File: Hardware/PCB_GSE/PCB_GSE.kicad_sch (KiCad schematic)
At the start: 0 parts

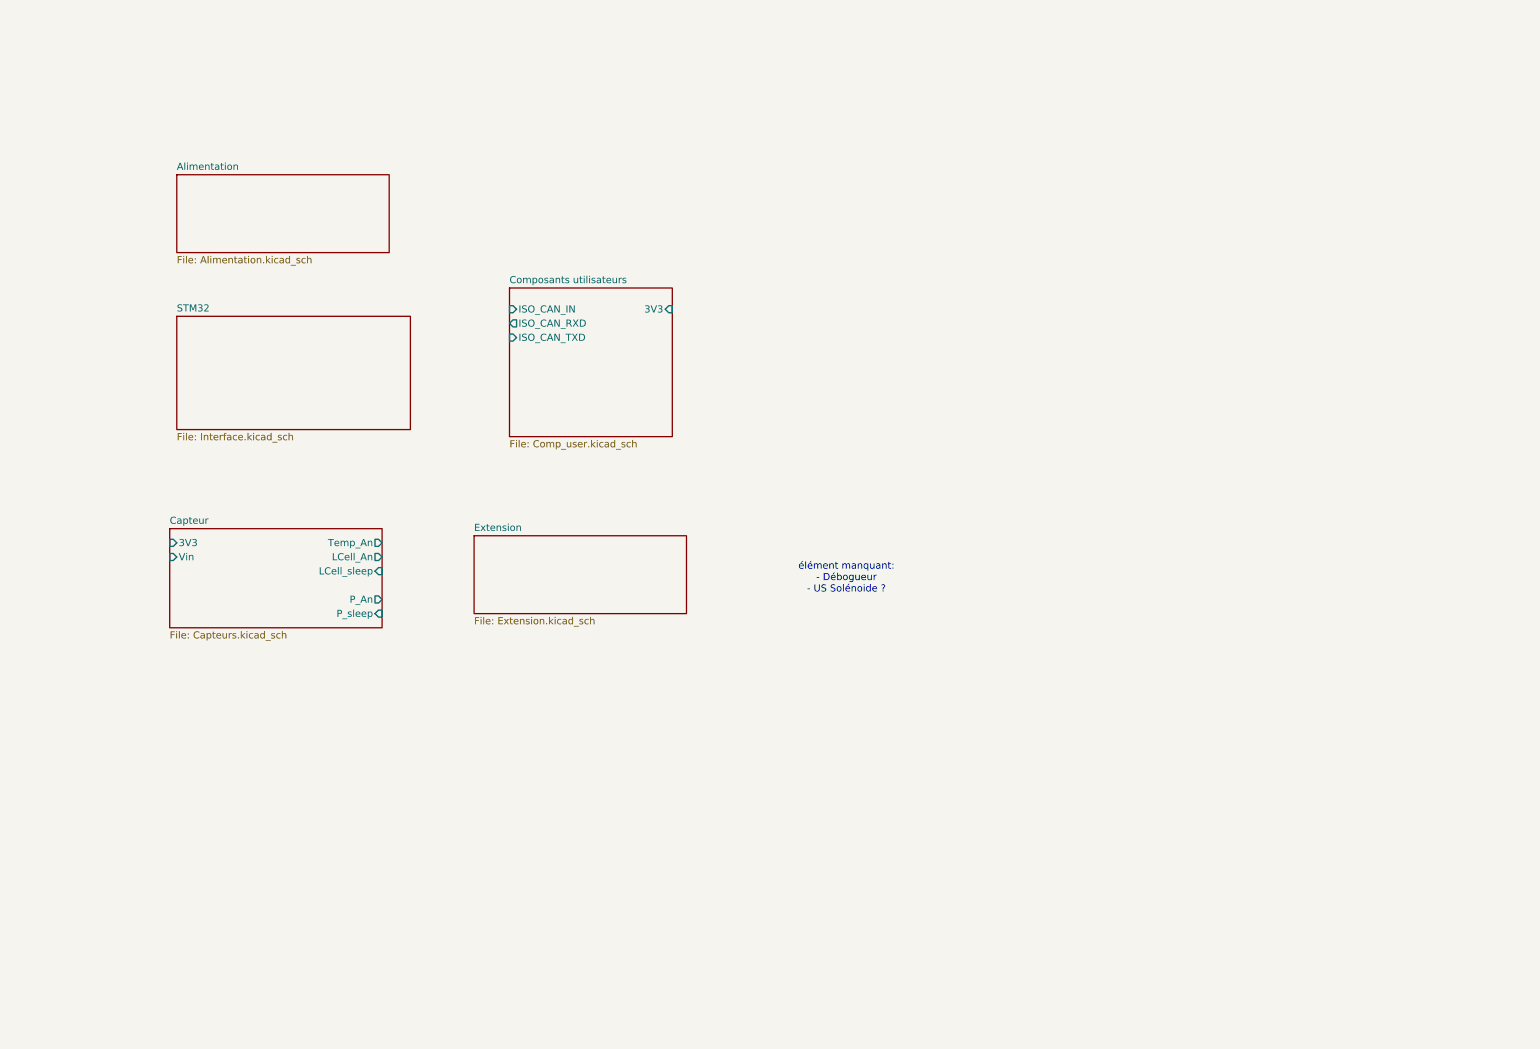
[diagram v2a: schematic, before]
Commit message: feat: copy all existing schematics in gse project + add missing components + fix voltage divider for 3S + create gse project and seperate stm32 project + add missing resistors motor
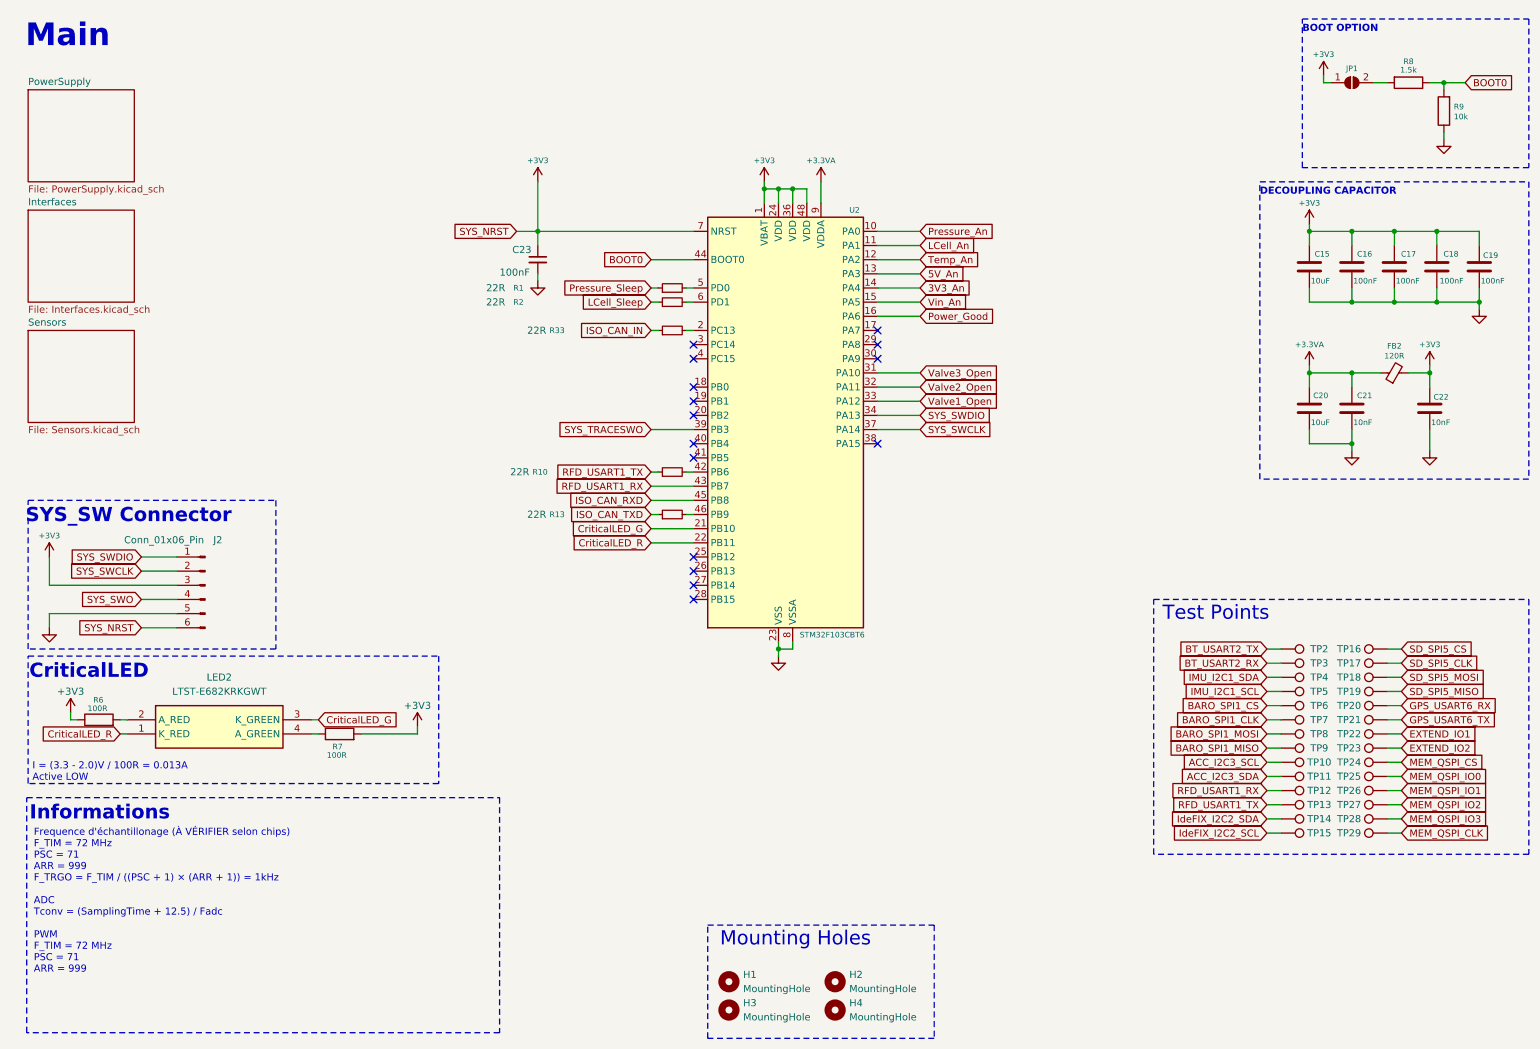
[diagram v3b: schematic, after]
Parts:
- added C15, C20: 10uF, Capacitor_SMD:C_0805_2012Metric, symbol Device:C
- added C16, C17, C18, C19: 100nF, Capacitor_SMD:C_0805_2012Metric, symbol Device:C
- added C21, C22: 10nF, Capacitor_SMD:C_0603_1608Metric, symbol Device:C
- added C23: 100nF, Capacitor_SMD:C_0805_2012Metric, symbol Device:C_Small
- added FB2: 120R, Inductor_SMD:L_0805_2012Metric, symbol Device:FerriteBead_Small
- added H1, H2, H3, H4: MountingHole, MountingHole:MountingHole_4.3mm_M4, symbol Mechanical:MountingHole
- added J2: Conn_01x06_Pin, Connector_PinHeader_2.54mm:PinHeader_1x06_P2.54mm_Vertical, symbol Connector:Conn_01x06_Pin
- added JP1: SolderJumper_2_Open, Jumper:SolderJumper-2_P1.3mm_Open_TrianglePad1.0x1.5mm, symbol Jumper:SolderJumper_2_Open
- added LED2: LTST-E682KRKGWT, LTSTE683RGBW, symbol PCB_GSE:LTST-E682KRKGWT
- added R1, R10, R13, R2, R33: 22R, Resistor_SMD:R_0603_1608Metric, symbol Device:R_Small
- added R6, R7: 100R, Resistor_SMD:R_0805_2012Metric, symbol Device:R
- added R8: 1.5k, Resistor_SMD:R_0603_1608Metric, symbol Device:R
- added R9: 10k, Resistor_SMD:R_0603_1608Metric, symbol Device:R
- added TP10, TP11, TP12, TP13, TP14, TP15, TP16, TP17, TP18, TP19, TP2, TP20, TP21, TP22, TP23, TP24, TP25, TP26, TP27, TP28, TP29, TP3, TP4, TP5, TP6, TP7, TP8, TP9: TestPoint, TestPoint:TestPoint_Pad_D1.0mm, symbol Connector:TestPoint
- added U2: STM32F103CBT6, Package_QFP:LQFP-48_7x7mm_P0.5mm, symbol MCU_ST_STM32F1:STM32F103C8Tx
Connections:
- new net: LED2.4 (A_GREEN), R7.1
- new net: R1.2, U2.5 (PD0)
- new net: R33.2, U2.2 (PC13)
- new net: R10.2, U2.42 (PB6)
- new net: R13.2, U2.46 (PB9)
- new net: R2.2, U2.6 (PD1)
- new net: JP1.2 (B), R8.2
- new net: LED2.2 (A_RED), R6.2
- new net +3.3VA: C20.2, C21.2, FB2.1, U2.9 (VDDA)
- new net +3V3: C15.2, C16.2, C17.2, C18.2, C19.2, C22.2, C23.1, FB2.2, J2.3 (Pin_3), J2.6 (Pin_6), JP1.1 (A), R6.1, R7.2, U2.1 (VBAT), U2.24 (VDD), U2.36 (VDD), U2.48 (VDD), U2.7 (NRST)
- new net 3V3_An: U2.14 (PA4)
- new net 5V_An: U2.13 (PA3)
- new net ACC_I2C3_SCL: TP10.1
- new net ACC_I2C3_SDA: TP11.1
- new net BARO_SPI1_CLK: TP7.1
- new net BARO_SPI1_CS: TP6.1
- new net BARO_SPI1_MISO: TP9.1
- new net BARO_SPI1_MOSI: TP8.1
- new net BOOT0: R8.1, R9.2, U2.44 (BOOT0)
- new net BT_USART2_RX: TP3.1
- new net BT_USART2_TX: TP2.1
- new net CriticalLED_G: LED2.3 (K_GREEN), U2.21 (PB10)
- new net CriticalLED_R: LED2.1 (K_RED), U2.22 (PB11)
- new net EXTEND_IO1: TP22.1
- new net EXTEND_IO2: TP23.1
- new net GND: C15.1, C16.1, C17.1, C18.1, C19.1, C20.1, C21.1, C22.1, C23.2, J2.5 (Pin_5), R9.1, U2.23 (VSS), U2.35 (VSS), U2.47 (VSS), U2.8 (VSSA)
- new net GPS_USART6_RX: TP20.1
- new net GPS_USART6_TX: TP21.1
- new net IMU_I2C1_SCL: TP5.1
- new net IMU_I2C1_SDA: TP4.1
- new net ISO_CAN_IN: R33.1
- new net ISO_CAN_RXD: U2.45 (PB8)
- new net ISO_CAN_TXD: R13.1
- new net IdeFIX_I2C2_SCL: TP15.1
- new net IdeFIX_I2C2_SDA: TP14.1
- new net LCell_An: U2.11 (PA1)
- new net LCell_Sleep: R2.1
- new net MEM_QSPI_CLK: TP29.1
- new net MEM_QSPI_CS: TP24.1
- new net MEM_QSPI_IO0: TP25.1
- new net MEM_QSPI_IO1: TP26.1
- new net MEM_QSPI_IO2: TP27.1
- new net MEM_QSPI_IO3: TP28.1
- new net Power_Good: U2.16 (PA6)
- new net Pressure_An: U2.10 (PA0)
- new net Pressure_Sleep: R1.1
- new net RFD_USART1_RX: TP12.1, U2.43 (PB7)
- new net RFD_USART1_TX: R10.1, TP13.1
- new net SD_SPI5_CLK: TP17.1
- new net SD_SPI5_CS: TP16.1
- new net SD_SPI5_MISO: TP19.1
- new net SD_SPI5_MOSI: TP18.1
- new net SYS_SWCLK: J2.2 (Pin_2), U2.37 (PA14)
- new net SYS_SWDIO: J2.1 (Pin_1), U2.34 (PA13)
- new net SYS_SWO: J2.4 (Pin_4)
- new net SYS_TRACESWO: U2.39 (PB3)
- new net Temp_An: U2.12 (PA2)
- new net Valve1_Open: U2.33 (PA12)
- new net Valve2_Open: U2.32 (PA11)
- new net Valve3_Open: U2.31 (PA10)
- new net Vin_An: U2.15 (PA5)
- no-connect marks 0 -> 15
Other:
- removed sheet Alimentation
- removed sheet Capteur
- removed sheet Composants utilisateurs
- removed sheet Extension
- removed sheet STM32
- added sheet Interfaces (Interfaces.kicad_sch)
- added sheet PowerSupply (PowerSupply.kicad_sch)
- added sheet Sensors (Sensors.kicad_sch)
- note added: "BOOT OPTION"
- note added: "CriticalLED"
- note added: "DECOUPLING CAPACITOR"
- note added: "Frequence d'échantillonage (À VÉRIFIER selon chips) F_TIM = 72 MHz PSC = 71 ARR = 999 F_TRGO = F_TIM / ((PSC + 1) × (ARR + 1)) = 1kHz ADC Tconv = (SamplingTime + 12.5) / Fadc PWM F_TIM = 72 MHz PSC = 71 ARR = 999"
- note added: "I = (3.3 - 2.0)V / 100R = 0.013A Active LOW"
- note added: "Informations"
- note added: "Main"
- note added: "Mounting Holes"
- note added: "SYS_SW Connector"
- note added: "Test Points"
- note removed: "élément manquant: - Débogueur - US Solénoide ?"

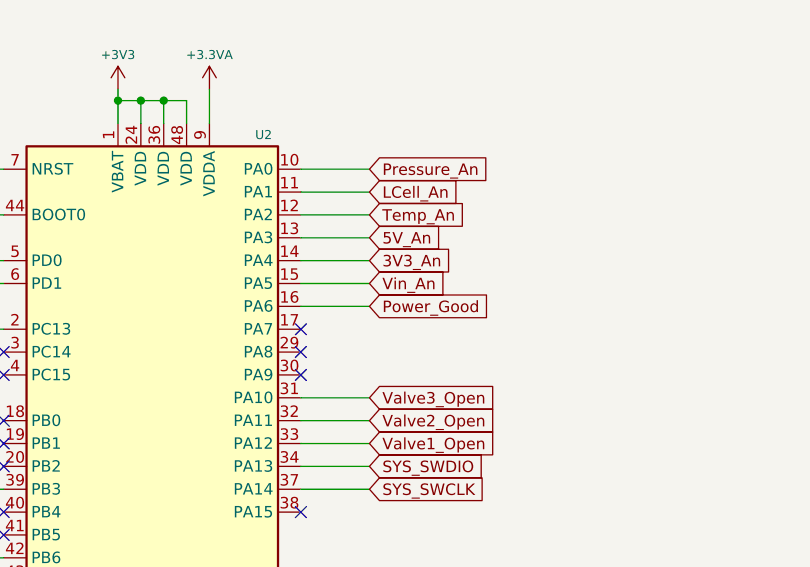
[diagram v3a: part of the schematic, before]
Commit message: fix: stm32 project + modified 12v buck symbol
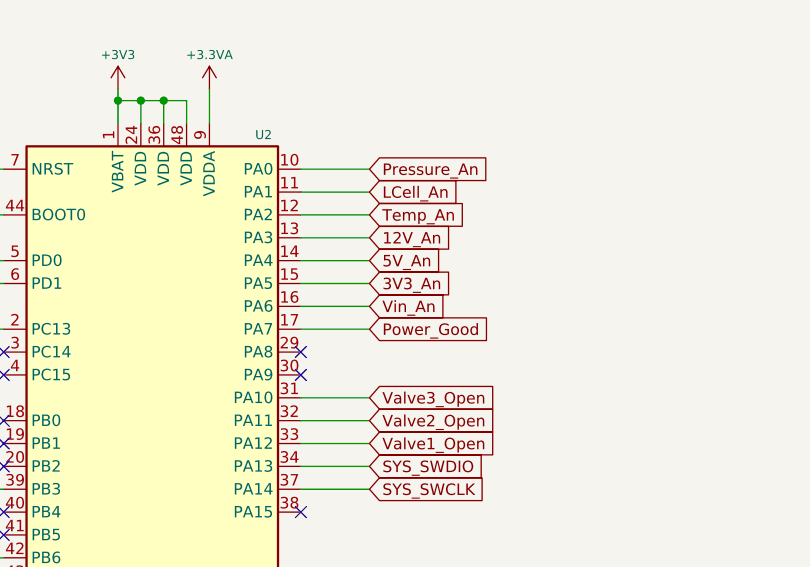
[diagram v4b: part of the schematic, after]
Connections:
- net 3V3_An: now also U2.15 (PA5); no longer U2.14 (PA4)
- net 5V_An: now also U2.14 (PA4); no longer U2.13 (PA3)
- net Power_Good: now also U2.17 (PA7); no longer U2.16 (PA6)
- net Vin_An: now also U2.16 (PA6); no longer U2.15 (PA5)
- new net 12V_An: U2.13 (PA3)
- no-connect marks 15 -> 14

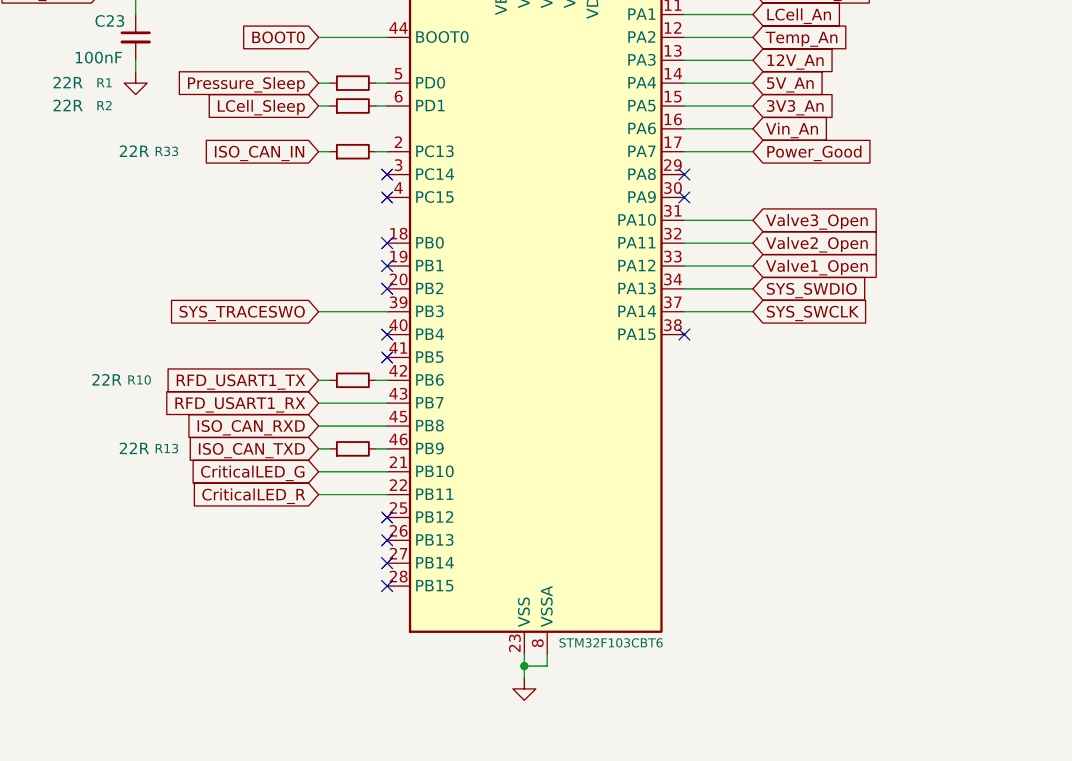
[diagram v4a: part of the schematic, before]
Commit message: feat: add extended ios + add stm32 project extended ios +
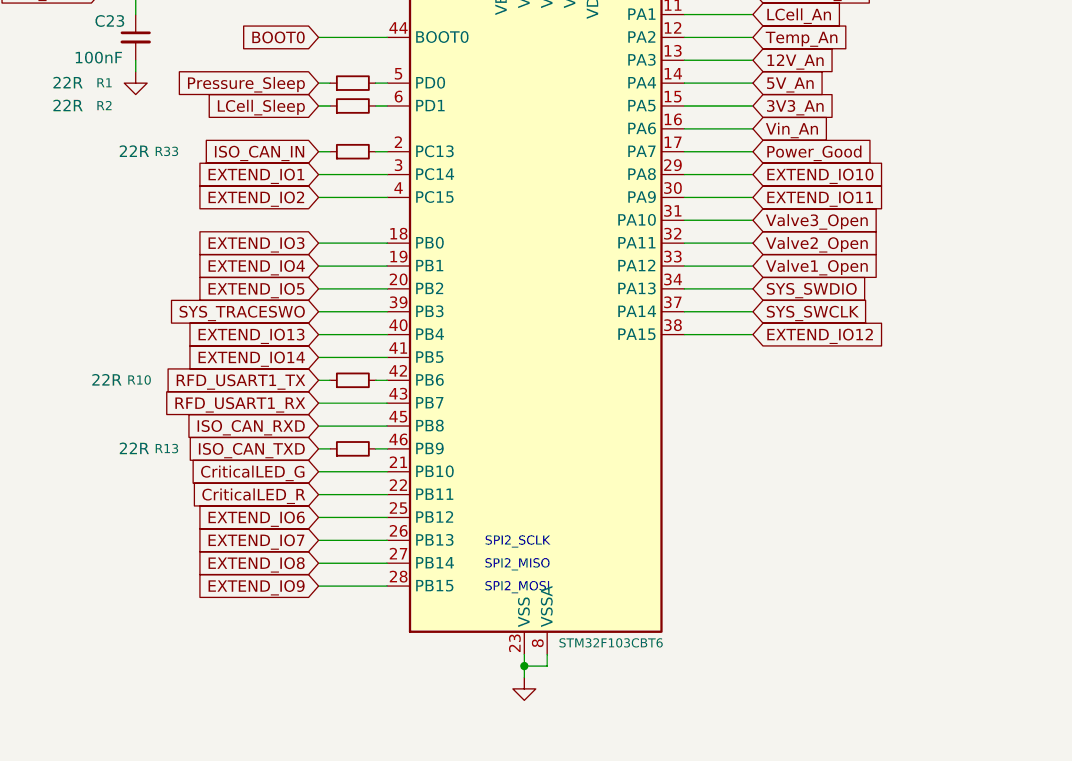
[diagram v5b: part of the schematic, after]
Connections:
- net EXTEND_IO1: now also U2.3 (PC14)
- net EXTEND_IO2: now also U2.4 (PC15)
- net EXTEND_IO3: now reaches U2.18 (PB0)
- net EXTEND_IO4: now reaches U2.19 (PB1)
- net EXTEND_IO5: now reaches U2.20 (PB2)
- net EXTEND_IO6: now reaches U2.25 (PB12)
- net EXTEND_IO7: now reaches U2.26 (PB13)
- net EXTEND_IO8: now reaches U2.27 (PB14)
- net EXTEND_IO9: now reaches U2.28 (PB15)
- net EXTEND_IO10: now reaches U2.29 (PA8)
- net EXTEND_IO11: now reaches U2.30 (PA9)
- net EXTEND_IO12: now reaches U2.38 (PA15)
- net EXTEND_IO13: now reaches U2.40 (PB4)
- net EXTEND_IO14: now reaches U2.41 (PB5)
- no-connect marks 14 -> 0
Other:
- note added: "SPI2_MISO"
- note added: "SPI2_MOSI"
- note added: "SPI2_SCLK"

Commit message: refactor: merge emile + main branches
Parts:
- removed R33: 22R, Resistor_SMD:R_0603_1608Metric, symbol Device:R_Small
- renumbered C23 to C1, C15 to C2, C20 to C3, C16 to C4, C21 to C5, C17 to C6, C22 to C7, C18 to C8, C19 to C9, FB2 to FB1, H3 to H2, H2 to H3, J2 to J1, LED2 to LED1, R6 to R1, R7 to R2, R1 to R3, R2 to R4, R10 to R6, R13 to R7, TP2 to TP1, TP11 to TP10, TP12 to TP11, TP13 to TP12, TP14 to TP13, TP15 to TP14, TP16 to TP15, TP17 to TP16, TP18 to TP17, TP19 to TP18, TP20 to TP19, TP3 to TP2, TP21 to TP20, TP22 to TP21, TP23 to TP22, TP24 to TP23, TP25 to TP24, TP26 to TP25, TP27 to TP26, TP28 to TP27, TP29 to TP28, TP4 to TP3, TP5 to TP4, TP6 to TP5, TP7 to TP6, TP8 to TP7, TP9 to TP8, TP10 to TP9, U2 to U1
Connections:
- net SYS_TRACESWO is gone; now on net SYS_SWO: U1.39 (PB3)
- net +3V3: no longer C2.2, C4.2, C6.2, C8.2, C9.2
- net ISO_CAN_OUT: now reaches U1.2 (PC13)
- new net: C2.2, C4.2, C6.2, C8.2, C9.2

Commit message: fix: labels
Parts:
- removed TP10, TP11, TP12, TP13, TP14, TP17, TP18, TP19, TP20, TP21, TP22, TP23, TP24, TP25, TP26, TP27, TP28, TP3, TP4, TP5, TP6, TP7, TP8, TP9: TestPoint, TestPoint:TestPoint_Pad_D1.0mm, symbol Connector:TestPoint
- added R3: 10k, Resistor_SMD:R_0603_1608Metric, symbol Device:R_Small
- renumbered R3 to R4, R4 to R5
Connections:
- net +3V3: now also R3.1; no longer C1.1, J1.6 (Pin_6), U1.7 (NRST)
- new net SYS_NRST: C1.1, J1.6 (Pin_6), R3.2, U1.7 (NRST)

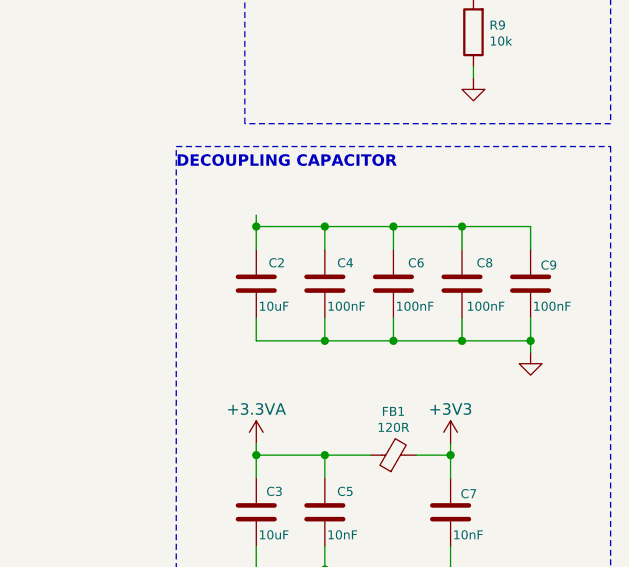
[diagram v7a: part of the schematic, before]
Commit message: fix: decoupling 3v3 missing
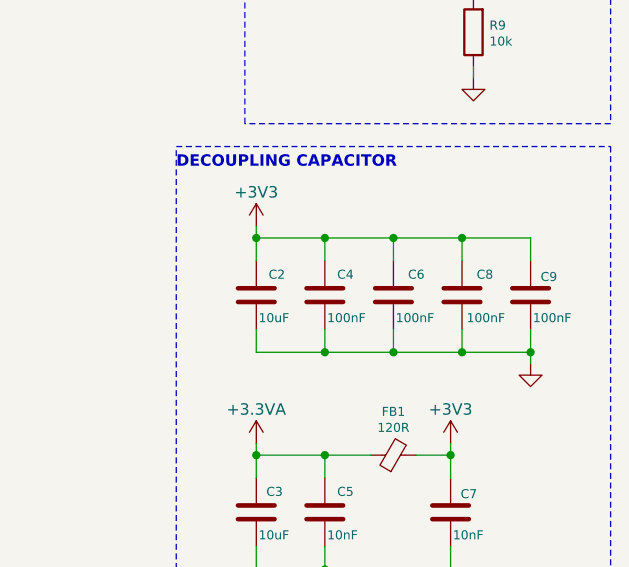
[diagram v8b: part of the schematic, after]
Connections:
- net +3V3: now also C2.2, C4.2, C6.2, C8.2, C9.2
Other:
- moved on the sheet: C2, C4, C6, C8, C9
